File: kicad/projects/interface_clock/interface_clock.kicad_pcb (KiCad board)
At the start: 2 copper layers, 203.2 x 97.8 mm, 77 parts, among them J1 Control_signal_backplane, J10 Conn_01x02_Female, J2 Aux_connection, J3 Bus_connection, J4 MAR_content_in, J5 EXT BUS, J6 CONTROL_INPUTS, J7 CLOCK_RWMEM_OUT, J8 EXT ADDR, J9 Conn_01x03_Male, U1 74HC02, U10 74HC157, U11 74HC14, U12 74HC245, U13 74HC126, U14 74HC109, U2 74HC04, U3 74HC08, U4 74HC08, U5 74HC02, U6 74HC245, U7 74HC245, U8 74HC245, U9 74HC245, X1 CXO_DIP8

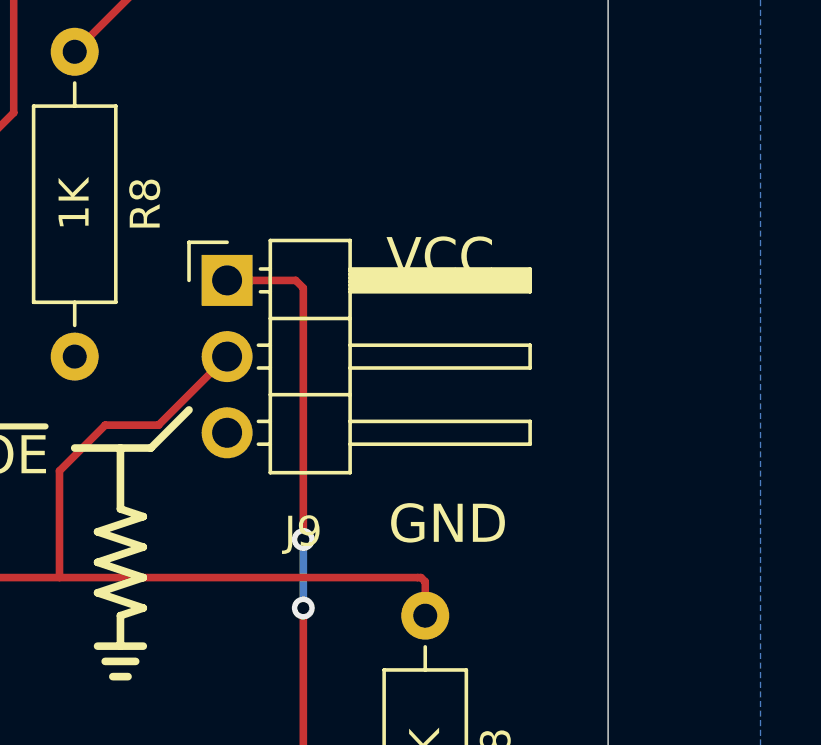
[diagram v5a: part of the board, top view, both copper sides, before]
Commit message: Added ECNZ to CPU Status.
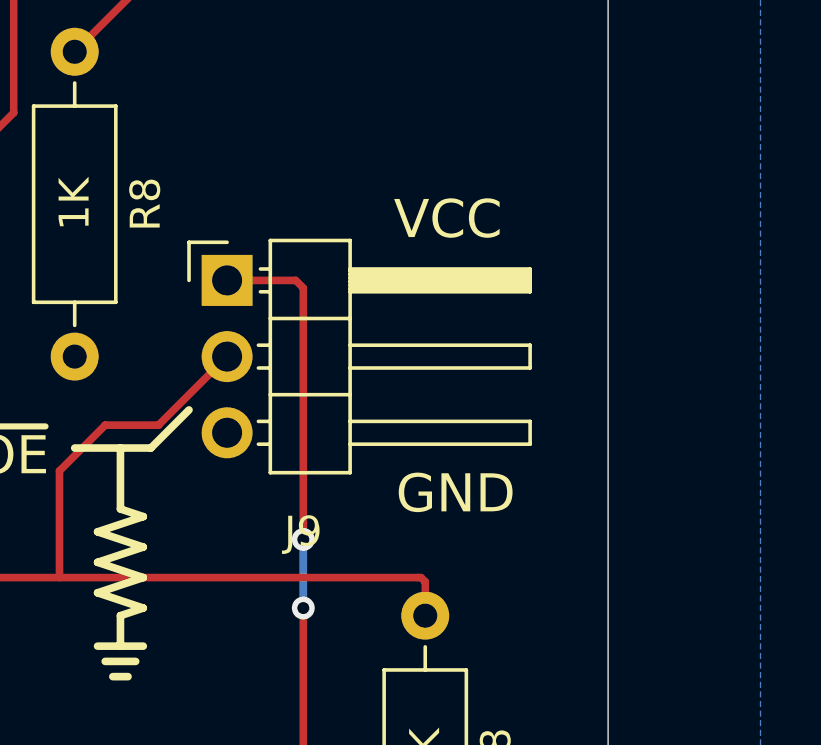
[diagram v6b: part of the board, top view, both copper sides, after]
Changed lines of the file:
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@@
     (effects (font (size 1.27 1.27) (thickness 0.2032)))
   )
-  (gr_text GND (at 248.666 86.868) (layer F.SilkS)
+  (gr_text GND (at 248.92 85.852) (layer F.SilkS)
     (effects (font (size 1.27 1.27) (thickness 0.2032)))
   )
-  (gr_text VCC (at 248.412 77.978) (layer F.SilkS)
+  (gr_text VCC (at 248.666 76.708) (layer F.SilkS)
     (effects (font (size 1.27 1.27) (thickness 0.2032)))
   )
@@
   (segment (start 220.618019 77.014962) (end 229.87 67.762981) (width 0.254) (layer F.Cu) (net 152))
   (segment (start 220.618019 84.181981) (end 220.618019 77.014962) (width 0.254) (layer F.Cu) (net 152))
-  (segment (start 234.188 65.532) (end 235.320001 64.399999) (width 0.254) (layer F.Cu) (net 170))
-  (segment (start 220.98 86.36) (end 234.188 73.152) (width 0.254) (layer F.Cu) (net 170))
-  (segment (start 235.320001 64.399999) (end 236.22 63.5) (width 0.254) (layer F.Cu) (net 170))
-  (segment (start 234.188 73.152) (end 234.188 65.532) (width 0.254) (layer F.Cu) (net 170))
   (via (at 220.726 110.49) (size 0.762) (drill 0.4) (layers F.Cu B.Cu) (net 153))
   (segment (start 220.726 110.49) (end 220.726 101.346) (width 0.254) (layer B.Cu) (net 153))
@@
   (segment (start 178.054 103.886) (end 192.278 103.886) (width 0.254) (layer F.Cu) (net 158))
   (via (at 192.278 103.886) (size 0.762) (drill 0.4) (layers F.Cu B.Cu) (net 158))
-  (via (at 208.28 120.904) (size 0.762) (drill 0.4) (layers F.Cu B.Cu) (net 171))
-  (segment (start 209.55 122.174) (end 208.28 120.904) (width 0.254) (layer F.Cu) (net 171))
-  (segment (start 210.058 125.984) (end 209.55 125.476) (width 0.254) (layer F.Cu) (net 171))
-  (segment (start 213.36 124.46) (end 211.836 125.984) (width 0.254) (layer F.Cu) (net 171))
-  (segment (start 209.55 125.476) (end 209.55 122.174) (width 0.254) (layer F.Cu) (net 171))
-  (segment (start 211.836 125.984) (end 210.058 125.984) (width 0.254) (layer F.Cu) (net 171))
-  (segment (start 208.28 114.3) (end 208.28 117.602) (width 0.254) (layer F.Cu) (net 171))
-  (segment (start 208.28 120.904) (end 208.28 117.602) (width 0.254) (layer B.Cu) (net 171))
-  (via (at 208.28 117.602) (size 0.762) (drill 0.4) (layers F.Cu B.Cu) (net 171))
   (via (at 200.66 116.078) (size 0.762) (drill 0.4) (layers F.Cu B.Cu) (net 159))
   (segment (start 200.66 116.078) (end 200.66 118.364) (width 0.254) (layer B.Cu) (net 159))
@@
   (segment (start 180.34 124.46) (end 186.944 124.46) (width 0.254) (layer F.Cu) (net 163))
   (segment (start 186.944 124.46) (end 187.198 124.714) (width 0.254) (layer F.Cu) (net 163))
+  (segment (start 234.188 65.532) (end 235.320001 64.399999) (width 0.254) (layer F.Cu) (net 170))
+  (segment (start 220.98 86.36) (end 234.188 73.152) (width 0.254) (layer F.Cu) (net 170))
+  (segment (start 235.320001 64.399999) (end 236.22 63.5) (width 0.254) (layer F.Cu) (net 170))
+  (segment (start 234.188 73.152) (end 234.188 65.532) (width 0.254) (layer F.Cu) (net 170))
+  (via (at 208.28 120.904) (size 0.762) (drill 0.4) (layers F.Cu B.Cu) (net 171))
+  (segment (start 209.55 122.174) (end 208.28 120.904) (width 0.254) (layer F.Cu) (net 171))
+  (segment (start 210.058 125.984) (end 209.55 125.476) (width 0.254) (layer F.Cu) (net 171))
+  (segment (start 213.36 124.46) (end 211.836 125.984) (width 0.254) (layer F.Cu) (net 171))
+  (segment (start 209.55 125.476) (end 209.55 122.174) (width 0.254) (layer F.Cu) (net 171))
+  (segment (start 211.836 125.984) (end 210.058 125.984) (width 0.254) (layer F.Cu) (net 171))
+  (segment (start 208.28 114.3) (end 208.28 117.602) (width 0.254) (layer F.Cu) (net 171))
+  (segment (start 208.28 120.904) (end 208.28 117.602) (width 0.254) (layer B.Cu) (net 171))
+  (via (at 208.28 117.602) (size 0.762) (drill 0.4) (layers F.Cu B.Cu) (net 171))
   (zone (net 1) (net_name GND) (layer B.Cu) (hatch edge 0.508)
     (connect_pads (clearance 0.508))

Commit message: interface tech checked.
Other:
- board text added: "ADDRESS"
- board text added: "ADDRESS BUS"
- board text removed: "ADDR BUS"
- board text removed: "ADDR IN"
